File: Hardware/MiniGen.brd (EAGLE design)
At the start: 17.8 x 33 mm, 32 parts, among them U1 16MHz, U2 3.3V, U3 AD9837

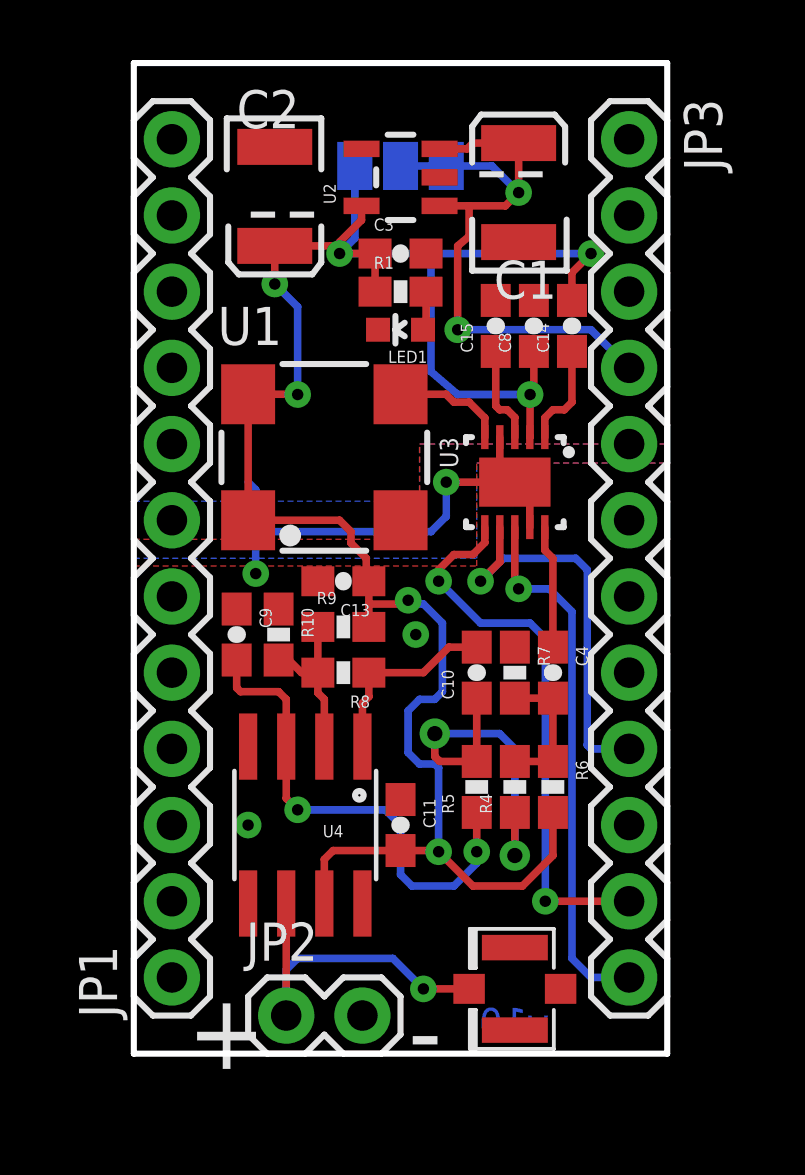
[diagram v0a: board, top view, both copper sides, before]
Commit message: added fiducials
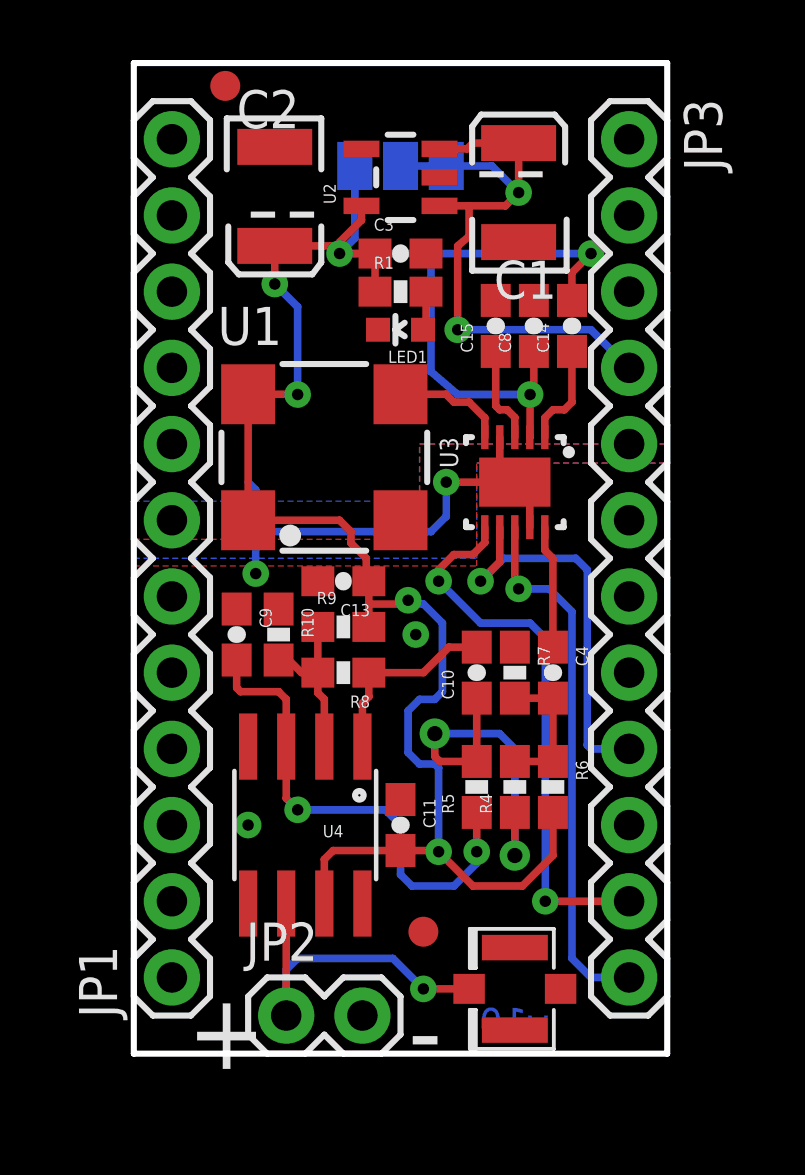
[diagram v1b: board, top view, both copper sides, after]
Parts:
- added FID1, FID2: FIDUCIAL1X2, SparkFun-Aesthetics:FIDUCIAL-1X2
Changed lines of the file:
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@@
 <?xml version="1.0" encoding="utf-8"?>
 <!DOCTYPE eagle SYSTEM "eagle.dtd">
-<eagle version="6.4">
+<eagle version="6.5.0">
 <drawing>
 <settings>
@@
 <setting verticaltext="up"/>
 </settings>
-<grid distance="0.05" unitdist="inch" unit="inch" style="lines" multiple="1" display="yes" altdistance="0.005" altunitdist="inch" altunit="inch"/>
+<grid distance="0.01" unitdist="inch" unit="inch" style="lines" multiple="1" display="yes" altdistance="0.001" altunitdist="inch" altunit="inch"/>
 <layers>
-<layer number="1" name="Top" color="4" fill="1" visible="no" active="yes"/>
-<layer number="2" name="Route2" color="1" fill="3" visible="no" active="yes"/>
-<layer number="15" name="Route15" color="4" fill="6" visible="no" active="yes"/>
+<layer number="1" name="Top" color="4" fill="1" visible="yes" active="yes"/>
+<layer number="2" name="Route2" color="1" fill="3" visible="yes" active="yes"/>
+<layer number="15" name="Route15" color="4" fill="6" visible="yes" active="yes"/>
 <layer number="16" name="Bottom" color="1" fill="1" visible="yes" active="yes"/>
 <layer number="17" name="Pads" color="2" fill="1" visible="yes" active="yes"/>
 <layer number="18" name="Vias" color="2" fill="1" visible="yes" active="yes"/>
 <layer number="19" name="Unrouted" color="6" fill="1" visible="yes" active="yes"/>
-<layer number="20" name="Dimension" color="15" fill="1" visible="yes" active="yes"/>
-<layer number="21" name="tPlace" color="16" fill="1" visible="no" active="yes"/>
-<layer number="22" name="bPlace" color="14" fill="1" visible="yes" active="yes"/>
-<layer number="23" name="tOrigins" color="15" fill="1" visible="no" active="yes"/>
+<layer number="20" name="Dimension" color="6" fill="1" visible="yes" active="yes"/>
+<layer number="21" name="tPlace" color="6" fill="1" visible="yes" active="yes"/>
+<layer number="22" name="bPlace" color="6" fill="1" visible="yes" active="yes"/>
+<layer number="23" name="tOrigins" color="15" fill="1" visible="yes" active="yes"/>
 <layer number="24" name="bOrigins" color="15" fill="1" visible="yes" active="yes"/>
-<layer number="25" name="tNames" color="7" fill="1" visible="no" active="yes"/>
-<layer number="26" name="bNames" color="7" fill="1" visible="no" active="yes"/>
-<layer number="27" name="tValues" color="7" fill="1" visible="no" active="yes"/>
-<layer number="28" name="bValues" color="7" fill="1" visible="no" active="yes"/>
-<layer number="29" name="tStop" color="7" fill="3" visible="no" active="yes"/>
-<layer number="30" name="bStop" color="7" fill="6" visible="no" active="yes"/>
-<layer number="31" name="tCream" color="7" fill="4" visible="no" active="yes"/>
-<layer number="32" name="bCream" color="7" fill="5" visible="no" active="yes"/>
-<layer number="39" name="tKeepout" color="4" fill="11" visible="no" active="yes"/>
-<layer number="40" name="bKeepout" color="1" fill="11" visible="no" active="yes"/>
-<layer number="41" name="tRestrict" color="4" fill="10" visible="no" active="yes"/>
-<layer number="42" name="bRestrict" color="1" fill="10" visible="no" active="yes"/>
-<layer number="43" name="vRestrict" color="2" fill="10" visible="no" active="yes"/>
-<layer number="44" name="Drills" color="7" fill="1" visible="no" active="yes"/>
-<layer number="45" name="Holes" color="7" fill="1" visible="no" active="yes"/>
-<layer number="46" name="Milling" color="3" fill="1" visible="no" active="yes"/>
-<layer number="51" name="tDocu" color="6" fill="1" visible="no" active="yes"/>
-<layer number="52" name="bDocu" color="7" fill="1" visible="no" active="yes"/>
+<layer number="25" name="tNames" color="7" fill="1" visible="yes" active="yes"/>
+<layer number="26" name="bNames" color="7" fill="1" visible="yes" active="yes"/>
+<layer number="27" name="tValues" color="7" fill="1" visible="yes" active="yes"/>
+<layer number="28" name="bValues" color="7" fill="1" visible="yes" active="yes"/>
+<layer number="29" name="tStop" color="7" fill="3" visible="yes" active="yes"/>
+<layer number="30" name="bStop" color="7" fill="6" visible="yes" active="yes"/>
+<layer number="31" name="tCream" color="7" fill="4" visible="yes" active="yes"/>
+<layer number="32" name="bCream" color="7" fill="5" visible="yes" active="yes"/>
+<layer number="39" name="tKeepout" color="4" fill="11" visible="yes" active="yes"/>
+<layer number="40" name="bKeepout" color="1" fill="11" visible="yes" active="yes"/>
+<layer number="41" name="tRestrict" color="4" fill="10" visible="yes" active="yes"/>
+<layer number="42" name="bRestrict" color="1" fill="10" visible="yes" active="yes"/>
+<layer number="43" name="vRestrict" color="2" fill="10" visible="yes" active="yes"/>
+<layer number="44" name="Drills" color="7" fill="1" visible="yes" active="yes"/>
+<layer number="45" name="Holes" color="7" fill="1" visible="yes" active="yes"/>
+<layer number="46" name="Milling" color="3" fill="1" visible="yes" active="yes"/>
+<layer number="51" name="tDocu" color="6" fill="1" visible="yes" active="yes"/>
+<layer number="52" name="bDocu" color="7" fill="1" visible="yes" active="yes"/>
 <layer number="3" name="Route3" color="4" fill="3" visible="no" active="no"/>
 <layer number="4" name="Route4" color="1" fill="4" visible="no" active="no"/>
@@
 </element>
 <element name="FRAME1" library="SparkFun-Aesthetics" package="CREATIVE_COMMONS" value="FRAME-LETTER" x="-5.95894375" y="-13.97"/>
+<element name="FID1" library="SparkFun-Aesthetics" package="FIDUCIAL-1X2" value="FIDUCIAL1X2" x="3.048" y="32.258"/>
+<element name="FID2" library="SparkFun-Aesthetics" package="FIDUCIAL-1X2" value="FIDUCIAL1X2" x="9.652" y="4.064"/>
 </elements>
 <signals>
